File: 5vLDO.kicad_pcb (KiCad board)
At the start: 2 copper layers, 7 parts, among them K1 CONN_3, K2 CONN_3, U1 AP1186K5

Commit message: unknown save
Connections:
- U1 pad 3: (no net) -> Vout
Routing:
- net Vout: track 38.2 -> 47.7 mm
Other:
- board text added: "2013 Visgence Inc"
- board text added: "5V LDO"
- board text added: "Gnd"
- board text added: "Vin"
- board text added: "Vout"
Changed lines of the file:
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@@
 (kicad_pcb (version 3) (host pcbnew "(2013-07-07 BZR 4022)-stable")
   (general
-    (links 14)
+    (links 15)
     (no_connects 1)
-    (area 0 0 0 0)
+    (area 41.579799 35.4076 63.9572 62.611001)
     (thickness 1.6)
-    (drawings 0)
-    (tracks 40)
+    (drawings 8)
+    (tracks 45)
     (zones 0)
     (modules 7)
@@
     (uvia_min_size 0.508)
     (uvia_min_drill 0.127)
-    (pcb_text_width 0.3)
-    (pcb_text_size 1.5 1.5)
+    (pcb_text_width 0.1)
+    (pcb_text_size 0.6 0.6)
     (mod_edge_width 0.15)
     (mod_text_size 1 1)
@@
     (pad 3 smd rect (at 0 12.53998 90) (size 3.79984 1.00076)
       (layers F.Cu F.Paste F.Mask)
+      (net 4 Vout)
     )
     (pad 4 smd rect (at 1.69926 12.53998 90) (size 3.7973 1.00076)
@@
     (descr "Connecteur 3 pins")
     (tags "CONN DEV")
-    (fp_text reference K1 (at 0.254 -2.159 270) (layer F.SilkS)
+    (fp_text reference K1 (at 5.588 -2.54 270) (layer F.SilkS) hide
       (effects (font (size 1.016 1.016) (thickness 0.1524)))
     )
@@
     (descr "Connecteur 3 pins")
     (tags "CONN DEV")
-    (fp_text reference K2 (at 0 2.286 270) (layer F.SilkS)
+    (fp_text reference K2 (at 4.826 0 270) (layer F.SilkS) hide
       (effects (font (size 1.016 1.016) (thickness 0.1524)))
     )
@@
     )
   )
+  (gr_text Vout (at 45.466 46.99) (layer F.SilkS)
+    (effects (font (size 0.6 0.6) (thickness 0.1)))
+  )
+  (gr_text Gnd (at 45.466 44.45) (layer F.SilkS)
+    (effects (font (size 0.6 0.6) (thickness 0.1)))
+  )
+  (gr_text Vin (at 45.466 41.148) (layer F.SilkS)
+    (effects (font (size 0.6 0.6) (thickness 0.1)))
+  )
+  (gr_text Vout (at 58.674 46.99) (layer F.SilkS)
+    (effects (font (size 0.6 0.6) (thickness 0.1)))
+  )
+  (gr_text Gnd (at 58.674 44.45) (layer F.SilkS)
+    (effects (font (size 0.5 0.5) (thickness 0.1)))
+  )
+  (gr_text Vin (at 58.674 41.148) (layer F.SilkS)
+    (effects (font (size 0.6 0.6) (thickness 0.1)))
+  )
+  (gr_text "5V LDO" (at 52.07 51.054) (layer B.SilkS)
+    (effects (font (size 1.5 1.5) (thickness 0.3)) (justify mirror))
+  )
+  (gr_text "2013\nVisgence Inc" (at 52.324 41.91) (layer B.SilkS)
+    (effects (font (size 1.5 1.5) (thickness 0.3)) (justify mirror))
+  )
   (segment (start 60.706 52.578) (end 51.054 52.578) (width 0.508) (layer B.Cu) (net 1))
-  (segment (start 43.9293 49.5427) (end 43.18 49.5427) (width 0.508) (layer F.Cu) (net 1) (status 800000))
+  (segment (start 43.9293 49.5427) (end 43.18 49.5427) (width 0.508) (layer F.Cu) (net 1))
   (segment (start 44.45 49.022) (end 43.9293 49.5427) (width 0.508) (layer F.Cu) (net 1))
   (via (at 44.45 49.022) (size 0.889) (layers F.Cu B.Cu) (net 1))
   (segment (start 47.498 49.022) (end 44.45 49.022) (width 0.508) (layer B.Cu) (net 1))
   (segment (start 51.054 52.578) (end 47.498 49.022) (width 0.508) (layer B.Cu) (net 1))
-  (segment (start 43.18 44.45) (end 60.96 44.45) (width 0.508) (layer B.Cu) (net 1) (status C00000))
-  (segment (start 60.96 44.45) (end 60.071002 44.45) (width 0.508) (layer F.Cu) (net 1) (status 400000))
-  (segment (start 60.96 58.928) (end 60.96 60.071) (width 0.508) (layer F.Cu) (net 1) (status 800000))
+  (segment (start 43.18 44.45) (end 60.96 44.45) (width 0.508) (layer B.Cu) (net 1))
+  (segment (start 60.96 44.45) (end 60.071002 44.45) (width 0.508) (layer F.Cu) (net 1))
+  (segment (start 60.96 58.928) (end 60.96 60.071) (width 0.508) (layer F.Cu) (net 1))
   (segment (start 60.706 58.674) (end 60.96 58.928) (width 0.508) (layer F.Cu) (net 1))
   (via (at 60.706 58.674) (size 0.889) (layers F.Cu B.Cu) (net 1))
@@
   (segment (start 44.45 60.071) (end 46.609 62.23) (width 0.762) (layer F.Cu) (net 1))
   (segment (start 43.18 52.832) (end 43.18 51.0413) (width 0.762) (layer F.Cu) (net 2))
-  (segment (start 43.18 41.91) (end 60.96 41.91) (width 0.508) (layer B.Cu) (net 3) (status C00000))
-  (segment (start 60.96 41.91) (end 59.944 41.91) (width 0.762) (layer F.Cu) (net 3) (status 400000))
+  (segment (start 43.18 41.91) (end 60.96 41.91) (width 0.508) (layer B.Cu) (net 3))
+  (segment (start 60.96 41.91) (end 59.944 41.91) (width 0.762) (layer F.Cu) (net 3))
   (segment (start 58.42 43.434) (end 58.42 57.15) (width 0.762) (layer F.Cu) (net 3))
   (segment (start 59.944 41.91) (end 58.42 43.434) (width 0.762) (layer F.Cu) (net 3))
@@
   (segment (start 57.31002 58.25998) (end 58.42 57.15) (width 0.762) (layer F.Cu) (net 3))
   (segment (start 58.42 57.15) (end 58.801 56.769) (width 0.762) (layer F.Cu) (net 3))
-  (segment (start 43.18 46.99) (end 60.96 46.99) (width 0.508) (layer B.Cu) (net 4) (status C00000))
+  (segment (start 48.66894 58.25998) (end 48.66894 55.21706) (width 0.508) (layer F.Cu) (net 4) (status 400000))
+  (segment (start 52.07 55.372) (end 52.07 58.25998) (width 0.508) (layer F.Cu) (net 4) (status 800000))
+  (segment (start 51.816 55.118) (end 52.07 55.372) (width 0.508) (layer F.Cu) (net 4))
+  (segment (start 48.768 55.118) (end 51.816 55.118) (width 0.508) (layer F.Cu) (net 4))
+  (segment (start 48.66894 55.21706) (end 48.768 55.118) (width 0.508) (layer F.Cu) (net 4))
+  (segment (start 43.18 46.99) (end 60.96 46.99) (width 0.508) (layer B.Cu) (net 4))
   (segment (start 43.18 46.99) (end 45.085 46.99) (width 0.762) (layer F.Cu) (net 4))
   (segment (start 45.72 47.625) (end 45.72 56.769) (width 0.762) (layer F.Cu) (net 4))

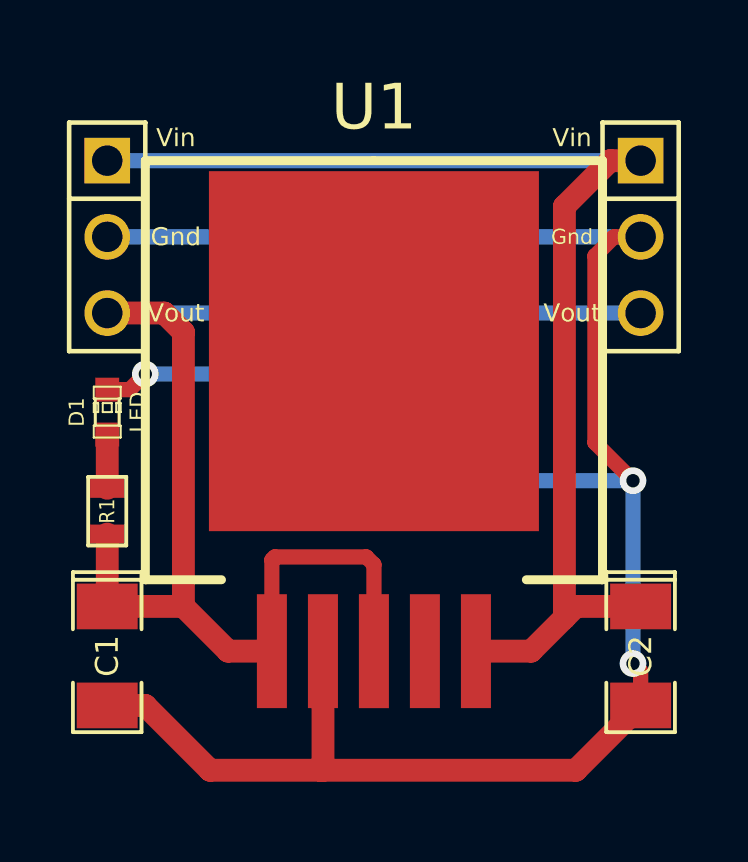
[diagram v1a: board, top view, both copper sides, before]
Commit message: Added edge, fixed missing trace
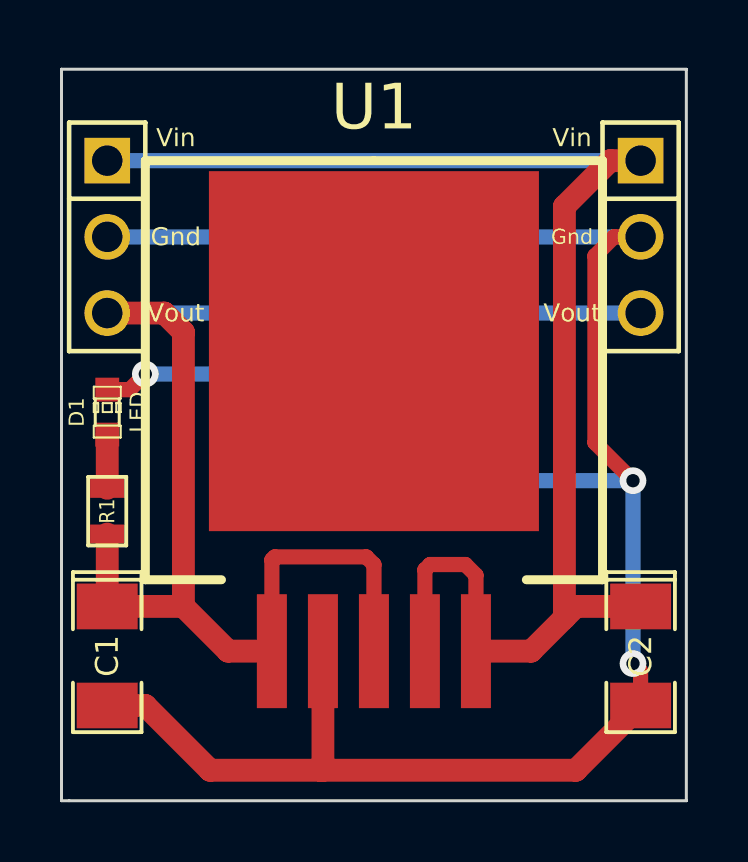
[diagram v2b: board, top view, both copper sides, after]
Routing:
- net Vin: track 40.8 -> 47.9 mm
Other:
- board outline added: 20.8 x 24.4 mm
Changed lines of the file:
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@@
   (general
     (links 15)
-    (no_connects 1)
+    (no_connects 0)
     (area 41.579799 35.4076 63.9572 62.611001)
     (thickness 1.6)
-    (drawings 8)
-    (tracks 45)
+    (drawings 13)
+    (tracks 50)
     (zones 0)
     (modules 7)
@@
     (pad_to_mask_clearance -0.0254)
     (aux_axis_origin 0 0)
-    (visible_elements FFFFFBBF)
+    (visible_elements 7FFFFFFF)
     (pcbplotparams
       (layerselection 3178497)
@@
     )
   )
+  (gr_line (start 41.656 63.246) (end 41.656 38.862) (angle 90) (layer Edge.Cuts) (width 0.1))
+  (gr_line (start 41.91 63.246) (end 41.656 63.246) (angle 90) (layer Edge.Cuts) (width 0.1))
+  (gr_line (start 62.484 63.246) (end 41.91 63.246) (angle 90) (layer Edge.Cuts) (width 0.1))
+  (gr_line (start 62.484 38.862) (end 62.484 63.246) (angle 90) (layer Edge.Cuts) (width 0.1))
+  (gr_line (start 41.656 38.862) (end 62.484 38.862) (angle 90) (layer Edge.Cuts) (width 0.1))
   (gr_text Vout (at 45.466 46.99) (layer F.SilkS)
     (effects (font (size 0.6 0.6) (thickness 0.1)))
@@
   (segment (start 44.45 60.071) (end 46.609 62.23) (width 0.762) (layer F.Cu) (net 1))
   (segment (start 43.18 52.832) (end 43.18 51.0413) (width 0.762) (layer F.Cu) (net 2))
+  (segment (start 53.76926 58.25998) (end 53.76926 55.54726) (width 0.508) (layer F.Cu) (net 3))
+  (segment (start 55.47106 55.72506) (end 55.47106 58.25998) (width 0.508) (layer F.Cu) (net 3))
+  (segment (start 55.118 55.372) (end 55.47106 55.72506) (width 0.508) (layer F.Cu) (net 3))
+  (segment (start 53.94452 55.372) (end 55.118 55.372) (width 0.508) (layer F.Cu) (net 3))
+  (segment (start 53.76926 55.54726) (end 53.94452 55.372) (width 0.508) (layer F.Cu) (net 3))
   (segment (start 43.18 41.91) (end 60.96 41.91) (width 0.508) (layer B.Cu) (net 3))
   (segment (start 60.96 41.91) (end 59.944 41.91) (width 0.762) (layer F.Cu) (net 3))
@@
   (segment (start 57.31002 58.25998) (end 58.42 57.15) (width 0.762) (layer F.Cu) (net 3))
   (segment (start 58.42 57.15) (end 58.801 56.769) (width 0.762) (layer F.Cu) (net 3))
-  (segment (start 48.66894 58.25998) (end 48.66894 55.21706) (width 0.508) (layer F.Cu) (net 4) (status 400000))
-  (segment (start 52.07 55.372) (end 52.07 58.25998) (width 0.508) (layer F.Cu) (net 4) (status 800000))
+  (segment (start 48.66894 58.25998) (end 48.66894 55.21706) (width 0.508) (layer F.Cu) (net 4))
+  (segment (start 52.07 55.372) (end 52.07 58.25998) (width 0.508) (layer F.Cu) (net 4))
   (segment (start 51.816 55.118) (end 52.07 55.372) (width 0.508) (layer F.Cu) (net 4))
   (segment (start 48.768 55.118) (end 51.816 55.118) (width 0.508) (layer F.Cu) (net 4))
